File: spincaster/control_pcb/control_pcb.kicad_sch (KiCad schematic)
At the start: 16 parts, among them J1 Extra, J2 Buzzer, J3 Relay, J4 Conn_01x05_Female, J5 Rocker, J6 PWR, SW2 IND_OFF, SW3 IND_ON, SW4 IND_PULSE, U1 LTV-817S, U2 LTV-817S, U3 LTV-817S

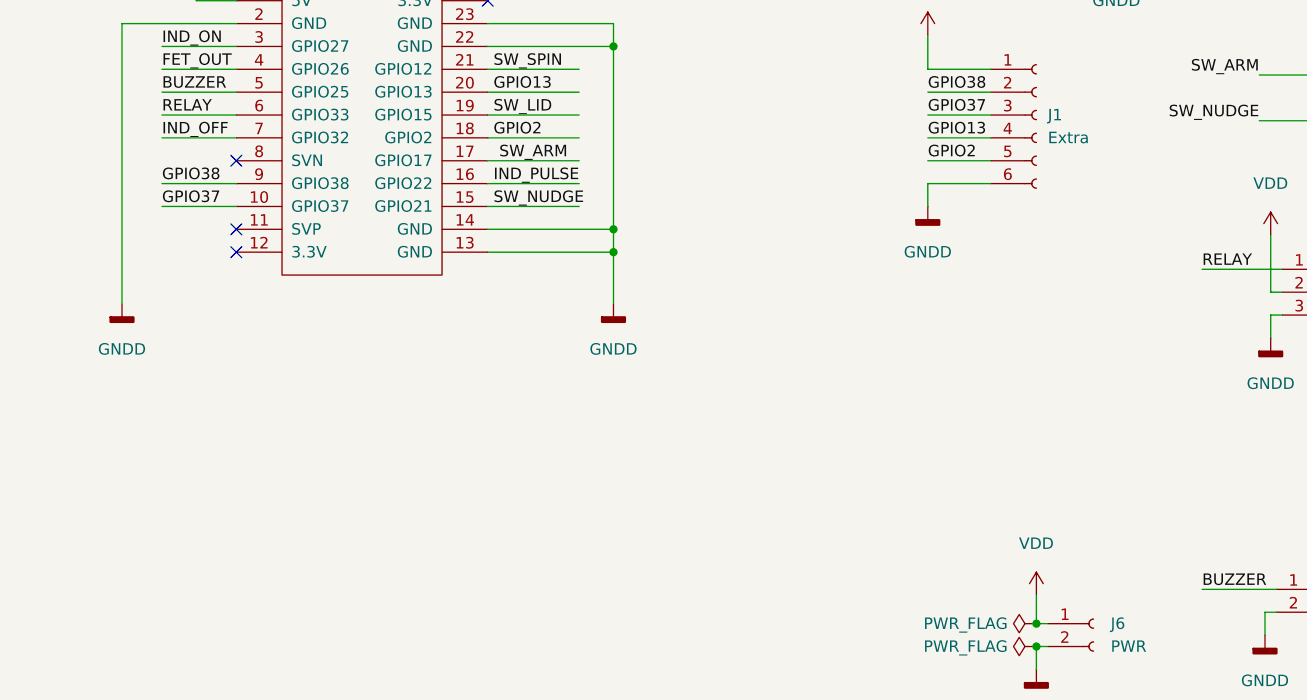
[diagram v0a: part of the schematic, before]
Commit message: Add O2 sensor logic to firmware, check in control PCB kicad updates and o2 sensor mount ipynb
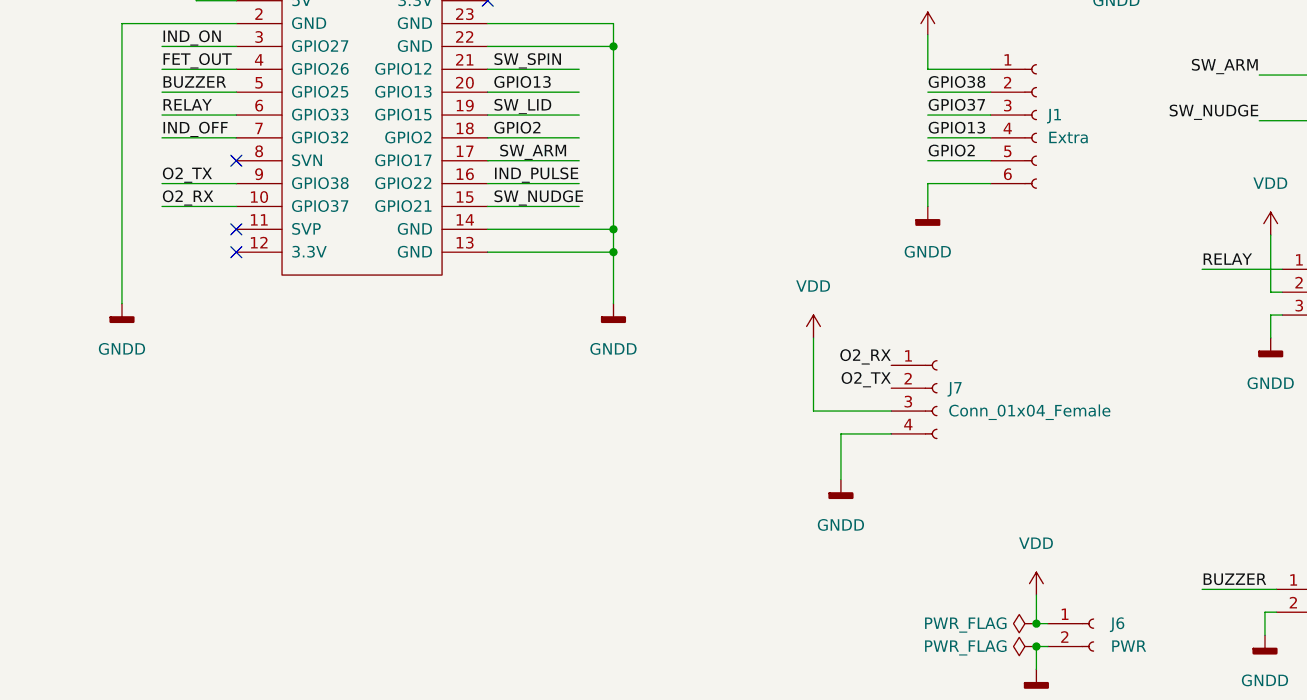
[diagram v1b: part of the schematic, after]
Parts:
- added J7: Conn_01x04_Female, Connector_JST:JST_PH_B4B-PH-K_1x04_P2.00mm_Vertical, symbol Connector:Conn_01x04_Female
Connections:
- net GNDD: now also J7.4 (Pin_4)
- net GPIO37: no longer TTGO1.10 (GPIO37)
- net GPIO38: no longer TTGO1.9 (GPIO38)
- net VDD: now also J7.3 (Pin_3)
- new net O2_RX: J7.1 (Pin_1), TTGO1.10 (GPIO37)
- new net O2_TX: J7.2 (Pin_2), TTGO1.9 (GPIO38)
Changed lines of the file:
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@@
+    (stroke (width 0) (type default) (color 0 0 0 0))
+  )
+  (wire (pts (xy 207.01 100.33) (xy 207.01 108.458))
     (stroke (width 0) (type default) (color 0 0 0 0))
   )
@@
     (stroke (width 0) (type default) (color 0 0 0 0))
   )
+  (wire (pts (xy 215.646 110.998) (xy 210.058 110.998))
+    (stroke (width 0) (type default) (color 0 0 0 0))
+  )
   (wire (pts (xy 257.81 97.79) (xy 257.81 100.33))
     (stroke (width 0) (type default) (color 0 0 0 0))
@@
     (stroke (width 0) (type default) (color 0 0 0 0))
   )
+  (wire (pts (xy 210.058 110.998) (xy 210.058 116.078))
+    (stroke (width 0) (type default) (color 0 0 0 0))
+  )
   (wire (pts (xy 82.55 95.25) (xy 90.17 95.25))
     (stroke (width 0) (type default) (color 0 0 0 0))
@@
     (stroke (width 0) (type default) (color 0 0 0 0))
   )
+  (wire (pts (xy 207.01 108.458) (xy 215.646 108.458))
+    (stroke (width 0) (type default) (color 0 0 0 0))
+  )
   (wire (pts (xy 233.045 134.62) (xy 231.775 134.62))
     (stroke (width 0) (type default) (color 0 0 0 0))
@@
   (label "GPIO2" (at 171.45 78.105 0)
     (effects (font (size 1.27 1.27)) (justify left bottom))
+  )
+  (label "O2_TX" (at 215.646 105.918 180)
+    (effects (font (size 1.27 1.27)) (justify right bottom))
   )
   (label "GPIO2" (at 219.71 80.645 0)
@@
     (effects (font (size 1.27 1.27)) (justify left bottom))
   )
-  (label "GPIO38" (at 134.62 83.185 0)
+  (label "O2_TX" (at 134.62 83.185 0)
     (effects (font (size 1.27 1.27)) (justify left bottom))
   )
@@
     (effects (font (size 1.27 1.27)) (justify left bottom))
   )
+  (label "O2_RX" (at 215.646 103.378 180)
+    (effects (font (size 1.27 1.27)) (justify right bottom))
+  )
   (label "SW_NUDGE" (at 256.54 76.2 180)
     (effects (font (size 1.27 1.27)) (justify right bottom))
@@
     (effects (font (size 1.27 1.27)) (justify right bottom))
   )
-  (label "GPIO37" (at 134.62 85.725 0)
+  (label "O2_RX" (at 134.62 85.725 0)
     (effects (font (size 1.27 1.27)) (justify left bottom))
   )
@@
     )
     (property "Datasheet" "" (id 3) (at 130.175 96.52 0)
+      (effects (font (size 1.27 1.27)) hide)
+    )
+    (pin "1")
+  )
+  (symbol (lib_id "power:GNDD") (at 210.058 116.078 0) (unit 1)
+    (in_bom yes) (on_board yes) (fields_autoplaced)
+    (property "Reference" "#PWR0120" (id 0) (at 210.058 122.428 0)
+      (effects (font (size 1.27 1.27)) hide)
+    )
+    (property "Value" "GNDD" (id 1) (at 210.058 121.158 0))
+    (property "Footprint" "" (id 2) (at 210.058 116.078 0)
+      (effects (font (size 1.27 1.27)) hide)
+    )
+    (property "Datasheet" "" (id 3) (at 210.058 116.078 0)
       (effects (font (size 1.27 1.27)) hide)
     )
@@
     (pin "1")
   )
+  (symbol (lib_id "power:VDD") (at 207.01 100.33 0) (unit 1)
+    (in_bom yes) (on_board yes) (fields_autoplaced)
+    (property "Reference" "#PWR0121" (id 0) (at 207.01 104.14 0)
+      (effects (font (size 1.27 1.27)) hide)
+    )
+    (property "Value" "VDD" (id 1) (at 207.01 94.615 0))
+    (property "Footprint" "" (id 2) (at 207.01 100.33 0)
+      (effects (font (size 1.27 1.27)) hide)
+    )
+    (property "Datasheet" "" (id 3) (at 207.01 100.33 0)
+      (effects (font (size 1.27 1.27)) hide)
+    )
+    (pin "1")
+  )
   (symbol (lib_id "power:PWR_FLAG") (at 66.675 96.52 270) (unit 1)
     (in_bom yes) (on_board yes) (fields_autoplaced)
@@
     )
     (pin "1")
+  )
+  (symbol (lib_id "Connector:Conn_01x04_Female") (at 220.726 105.918 0) (unit 1)
+    (in_bom yes) (on_board yes) (fields_autoplaced)
+    (property "Reference" "J7" (id 0) (at 221.996 105.9179 0)
+      (effects (font (size 1.27 1.27)) (justify left))
+    )
+    (property "Value" "Conn_01x04_Female" (id 1) (at 221.996 108.4579 0)
+      (effects (font (size 1.27 1.27)) (justify left))
+    )
+    (property "Footprint" "Connector_JST:JST_PH_B4B-PH-K_1x04_P2.00mm_Vertical" (id 2) (at 220.726 105.918 0)
+      (effects (font (size 1.27 1.27)) hide)
+    )
+    (property "Datasheet" "~" (id 3) (at 220.726 105.918 0)
+      (effects (font (size 1.27 1.27)) hide)
+    )
+    (pin "1")
+    (pin "2")
+    (pin "3")
+    (pin "4")
   )
   (symbol (lib_id "power:GND") (at 82.55 95.25 0) (unit 1)
@@
       (reference "#PWR0119") (unit 1) (value "GND") (footprint "")
     )
+    (path "/162b5d3a-0dcc-4218-a7e1-bdcf1300f666"
+      (reference "#PWR0120") (unit 1) (value "GNDD") (footprint "")
+    )
+    (path "/9e3d2cf8-92d8-4520-b210-cfda448eca5d"
+      (reference "#PWR0121") (unit 1) (value "VDD") (footprint "")
+    )
     (path "/5b3ee24b-caac-4bcc-93c6-9ea45a035fda"
       (reference "J1") (unit 1) (value "Extra") (footprint "Connector_PinHeader_2.54mm:PinHeader_1x06_P2.54mm_Vertical")
@@
       (reference "J6") (unit 1) (value "PWR") (footprint "Connector_JST:JST_PH_B2B-PH-K_1x02_P2.00mm_Vertical")
     )
+    (path "/af541b7f-47e2-4338-86d3-64a72b5b7aba"
+      (reference "J7") (unit 1) (value "Conn_01x04_Female") (footprint "Connector_JST:JST_PH_B4B-PH-K_1x04_P2.00mm_Vertical")
+    )
     (path "/0fc7e38d-0799-4e7f-93c6-eebfeec17e42"
